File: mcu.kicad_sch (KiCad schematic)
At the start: 24 parts, among them J10 Conn_01x16, J8 Conn_01x12, U3 W25Q64JVSSIQ, U9 MDBT50Q-1MV2, Y1 ABS06-32.768KHZ-1-T

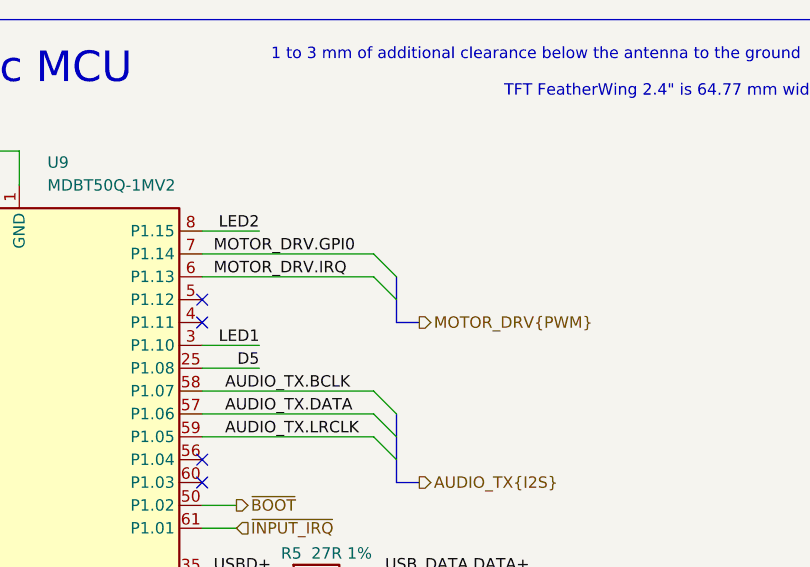
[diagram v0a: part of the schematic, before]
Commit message: Replaced DA7280 with DRV2605
Replaced DA7280 with DRV2605 to simplify board support code in Hack-A-Friend Arduino Library.
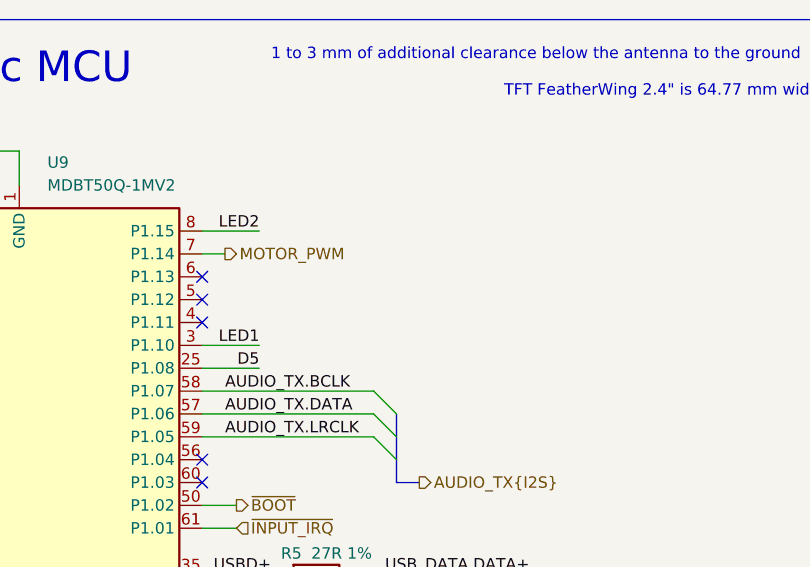
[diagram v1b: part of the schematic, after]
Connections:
- net MOTOR_DRV.GPI0 renamed MOTOR_PWM
- net MOTOR_DRV.IRQ: no longer names the net of U9.6 (P1.13)
- no-connect marks 5 -> 6
